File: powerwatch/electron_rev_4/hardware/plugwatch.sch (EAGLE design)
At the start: 124 parts, among them J1 DM3AT-SF-PEJM5, Q1 SI223DDS, Q2 MOSFET-NCHANNELSMD, U1 BGA725L6-ALT, U10 SIP32510, U12 SIP32510, U13 AB1815-T3, U16 MAX6746, U2 SAFFB1G56KB0F0A, U3 IRM-03-5V, U4 MAX-M8, U5 MAX9910, U6 LIS2DW12, U8 MAX9910, U9 SIP32510, X1 ABS07-32.768KHZ-7-T

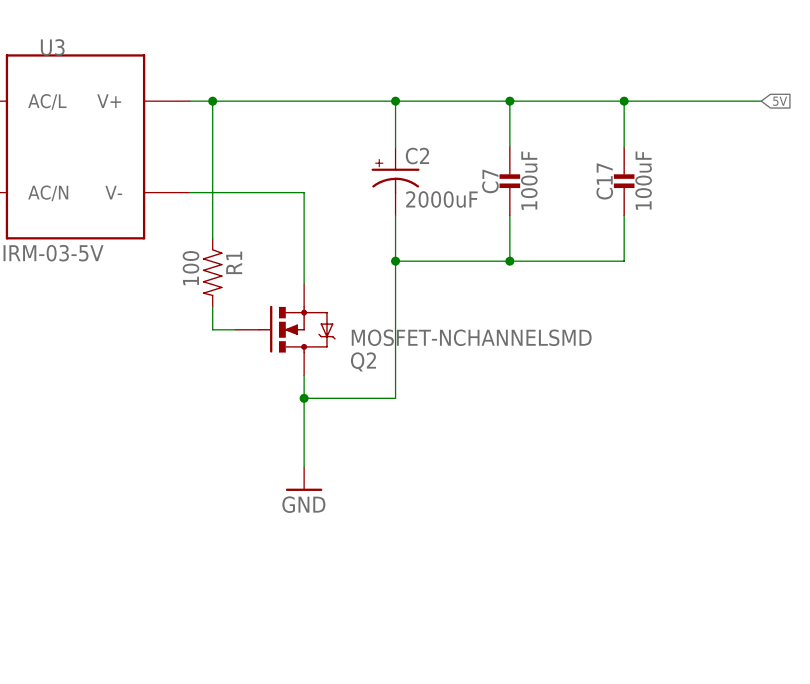
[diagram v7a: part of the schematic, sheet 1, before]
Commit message: a new mosfet configuration
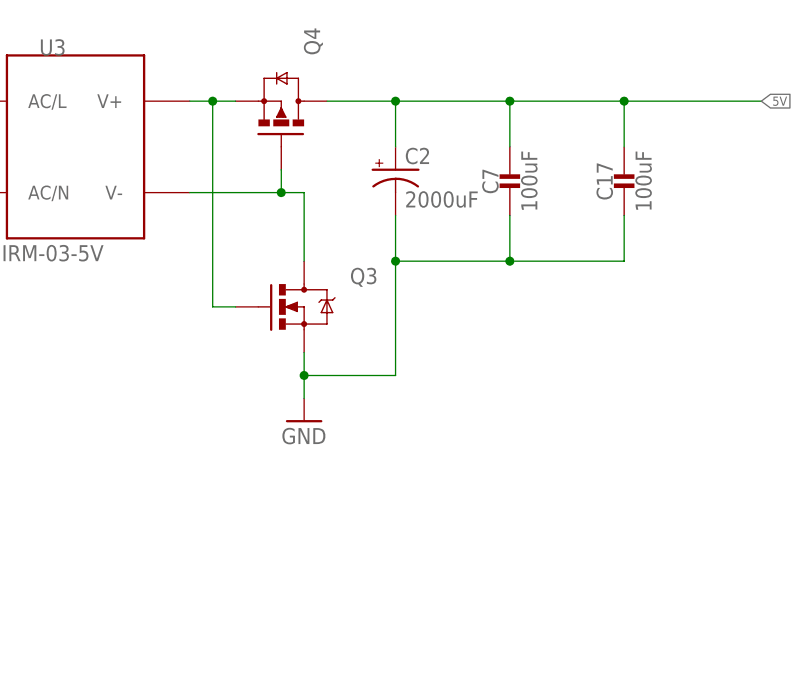
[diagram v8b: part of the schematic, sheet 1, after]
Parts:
- removed Q2: MOSFET-NCHANNELSMD, fets:MOSFET-NCHANNELSMD
- removed R1: 100, passives:RESISTOR0402_RES
- added Q3: MOSFET-NCHANNELSMD, fets:MOSFET-NCHANNELSMD
- added Q4: NX3008PBK, fets:NX3008PBK
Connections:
- net 5V: now also Q4.D; no longer R1.1, U3.V+
- net GND: now also Q3.S; no longer Q2.D
- net N$32: now also Q3.G, Q4.S, U3.V+; no longer Q2.G, R1.2
- net N$8: now also Q3.D, Q4.G; no longer Q2.S
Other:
- note removed: "Note that source is connected to V-...I am a bit unsure if this correct for the perturb circuit."
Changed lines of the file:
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@@
 <part name="C7" library="passives" deviceset="CAPACITOR" device="1210_CAP" value="100uF"/>
 <part name="C17" library="passives" deviceset="CAPACITOR" device="1210_CAP" value="100uF"/>
-<part name="Q2" library="fets" deviceset="MOSFET-NCHANNEL" device="SMD"/>
-<part name="R1" library="passives" deviceset="RESISTOR" device="0402_RES" value="100">
-<attribute name="DESCRIPTION" value="RES SMD 150 OHM 1% 1/16W 0402"/>
-<attribute name="DIGIKEY" value="RMCF0402FT150RCT-ND"/>
-<attribute name="MANUFACTURER" value="Stackpole Electronics"/>
-<attribute name="MPN" value="RMCF0402FT150R"/>
-</part>
 <part name="R7" library="varistor" library_urn="urn:adsk.eagle:library:410" deviceset="S14K385" device="" package3d_urn="urn:adsk.eagle:package:30572/1"/>
 <part name="F1" library="powerwatch" deviceset="MICRO_FUSE" device="500MA_350VAC" value="300VAC - 500ma"/>
@@
 <part name="TP16" library="headers" deviceset="TEST_POINT_0.040IN" device=""/>
 <part name="TP17" library="headers" deviceset="TEST_POINT_0.040IN" device=""/>
+<part name="Q3" library="fets" deviceset="MOSFET-NCHANNEL" device="SMD"/>
+<part name="Q4" library="fets" deviceset="NX3008PBK" device=""/>
 </parts>
 <sheets>
@@
 <text x="66.04" y="137.16" size="1.016" layer="98" align="bottom-center">We use a seperate AC Measure pin so that we can more directly sense the perturbation by the digital output.
 The full-scale voltage sensing circuit (below) could also be used, but would only sense &lt;1% of its dynamic range.</text>
-<text x="154.94" y="147.32" size="1.27" layer="98" align="bottom-center">Note that source is connected to V-...I am a bit unsure if this correct for the perturb circuit.</text>
 </plain>
 <instances>
@@
 <instance part="AC/L" gate="G$1" x="35.56" y="170.18"/>
 <instance part="AC/N" gate="G$1" x="35.56" y="147.32"/>
-<instance part="SUPPLY1" gate="1" x="142.24" y="127"/>
+<instance part="SUPPLY1" gate="1" x="142.24" y="134.62"/>
 <instance part="C2" gate="G$1" x="152.4" y="162.56"/>
 <instance part="C7" gate="G$1" x="165.1" y="162.56"/>
 <instance part="C17" gate="G$1" x="177.8" y="162.56"/>
-<instance part="Q2" gate="G$1" x="142.24" y="144.78" rot="MR180"/>
-<instance part="R1" gate="G$1" x="132.08" y="149.86" rot="R270">
-<attribute name="DIGIKEY" x="132.08" y="149.86" size="1.27" layer="96" rot="R270" display="off"/>
-</instance>
 <instance part="R7" gate="G$1" x="60.96" y="160.02" rot="R270"/>
 <instance part="F1" gate="G$1" x="48.26" y="170.18"/>
@@
 <attribute name="MANUFACTURER" x="93.98" y="119.38" size="1.016" layer="96" rot="R90" align="bottom-center" display="off"/>
 <attribute name="MPN" x="93.98" y="119.38" size="1.016" layer="96" rot="R90" align="bottom-center" display="off"/>
+</instance>
+<instance part="Q3" gate="G$1" x="142.24" y="147.32" smashed="yes">
+<attribute name="NAME" x="147.32" y="149.86" size="1.778" layer="95"/>
+</instance>
+<instance part="Q4" gate="G$1" x="139.7" y="170.18" smashed="yes" rot="MR90">
+<attribute name="NAME" x="142.24" y="175.26" size="1.778" layer="95" rot="MR90"/>
 </instance>
 </instances>
@@
 <net name="5V" class="0">
 <segment>
-<pinref part="U3" gate="G$1" pin="V+"/>
-<wire x1="129.54" y1="170.18" x2="132.08" y2="170.18" width="0.1524" layer="91"/>
 <label x="193.04" y="170.18" size="1.016" layer="95" xref="yes"/>
-<wire x1="132.08" y1="170.18" x2="152.4" y2="170.18" width="0.1524" layer="91"/>
 <wire x1="152.4" y1="170.18" x2="165.1" y2="170.18" width="0.1524" layer="91"/>
 <wire x1="165.1" y1="170.18" x2="177.8" y2="170.18" width="0.1524" layer="91"/>
 <wire x1="177.8" y1="170.18" x2="193.04" y2="170.18" width="0.1524" layer="91"/>
 <wire x1="152.4" y1="165.1" x2="152.4" y2="170.18" width="0.1524" layer="91"/>
-<junction x="152.4" y="170.18"/>
 <wire x1="165.1" y1="165.1" x2="165.1" y2="170.18" width="0.1524" layer="91"/>
 <junction x="165.1" y="170.18"/>
@@
 <pinref part="C7" gate="G$1" pin="1"/>
 <pinref part="C17" gate="G$1" pin="1"/>
-<pinref part="R1" gate="G$1" pin="1"/>
-<wire x1="132.08" y1="154.94" x2="132.08" y2="170.18" width="0.1524" layer="91"/>
-<junction x="132.08" y="170.18"/>
+<pinref part="Q4" gate="G$1" pin="D"/>
+<wire x1="144.78" y1="170.18" x2="152.4" y2="170.18" width="0.1524" layer="91"/>
+<junction x="152.4" y="170.18"/>
 </segment>
 </net>
@@
 <segment>
 <pinref part="SUPPLY1" gate="1" pin="GND"/>
-<wire x1="142.24" y1="129.54" x2="142.24" y2="137.16" width="0.1524" layer="91"/>
+<wire x1="142.24" y1="137.16" x2="142.24" y2="139.7" width="0.1524" layer="91"/>
 <wire x1="152.4" y1="157.48" x2="152.4" y2="152.4" width="0.1524" layer="91"/>
 <wire x1="165.1" y1="157.48" x2="165.1" y2="152.4" width="0.1524" layer="91"/>
@@
 <pinref part="C7" gate="G$1" pin="2"/>
 <pinref part="C17" gate="G$1" pin="2"/>
-<wire x1="152.4" y1="152.4" x2="152.4" y2="137.16" width="0.1524" layer="91"/>
+<wire x1="152.4" y1="152.4" x2="152.4" y2="139.7" width="0.1524" layer="91"/>
 <junction x="152.4" y="152.4"/>
-<wire x1="152.4" y1="137.16" x2="142.24" y2="137.16" width="0.1524" layer="91"/>
-<pinref part="Q2" gate="G$1" pin="D"/>
-<wire x1="142.24" y1="139.7" x2="142.24" y2="137.16" width="0.1524" layer="91"/>
-<junction x="142.24" y="137.16"/>
+<wire x1="152.4" y1="139.7" x2="142.24" y2="139.7" width="0.1524" layer="91"/>
+<junction x="142.24" y="139.7"/>
+<pinref part="Q3" gate="G$1" pin="S"/>
+<wire x1="142.24" y1="139.7" x2="142.24" y2="142.24" width="0.1524" layer="91"/>
 </segment>
 <segment>
@@
 <net name="N$32" class="0">
 <segment>
-<pinref part="R1" gate="G$1" pin="2"/>
-<wire x1="132.08" y1="144.78" x2="132.08" y2="147.32" width="0.1524" layer="91"/>
-<pinref part="Q2" gate="G$1" pin="G"/>
-<wire x1="132.08" y1="144.78" x2="134.62" y2="144.78" width="0.1524" layer="91"/>
+<pinref part="Q3" gate="G$1" pin="G"/>
+<wire x1="134.62" y1="147.32" x2="132.08" y2="147.32" width="0.1524" layer="91"/>
+<pinref part="U3" gate="G$1" pin="V+"/>
+<wire x1="129.54" y1="170.18" x2="132.08" y2="170.18" width="0.1524" layer="91"/>
+<wire x1="132.08" y1="147.32" x2="132.08" y2="170.18" width="0.1524" layer="91"/>
+<pinref part="Q4" gate="G$1" pin="S"/>
+<wire x1="132.08" y1="170.18" x2="134.62" y2="170.18" width="0.1524" layer="91"/>
+<junction x="132.08" y="170.18"/>
 </segment>
 </net>
@@
 <segment>
 <pinref part="U3" gate="G$1" pin="V-"/>
-<wire x1="129.54" y1="160.02" x2="142.24" y2="160.02" width="0.1524" layer="91"/>
-<pinref part="Q2" gate="G$1" pin="S"/>
-<wire x1="142.24" y1="149.86" x2="142.24" y2="160.02" width="0.1524" layer="91"/>
-</segment>
-</net>
+<wire x1="129.54" y1="160.02" x2="139.7" y2="160.02" width="0.1524" layer="91"/>
+<pinref part="Q3" gate="G$1" pin="D"/>
+<wire x1="139.7" y1="160.02" x2="142.24" y2="160.02" width="0.1524" layer="91"/>
+<wire x1="142.24" y1="152.4" x2="142.24" y2="160.02" width="0.1524" layer="91"/>
+<pinref part="Q4" gate="G$1" pin="G"/>
+<wire x1="139.7" y1="162.56" x2="139.7" y2="160.02" width="0.1524" layer="91"/>
+<junction x="139.7" y="160.02"/>
+</segment>
+</net>
